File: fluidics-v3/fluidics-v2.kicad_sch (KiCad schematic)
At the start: 33 parts, among them J1 PJ-063AH, J10 87832-1010, J11 0705430001, J12 87832-1010, J13 0705430001, J14 87832-1010, J15 0533980671, J16 0705430001, J17 0533980671, J18 87832-1010, J19 0705430001, J2 B6B-ZR-SM4-TF, J20 0533980671, J21 87832-1010, J22 0705430001, J24 0705430001, J25 87832-1010, J3 A-DS_15_A_KG-T4S, J4 B6B-ZR-SM4-TF, U2 Teensy4.1

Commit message: Add GPIO_5 status LED and +24V screw terminal J7
- Root sheet: GPIO_5 status LED (D12 + R12 2.7K to GND)
- Solenoid driver sheet: J7 2-pin screw terminal (pin2 = +24V)

Schematic parses clean via kicad-cli; D12/R12/J7 present in netlist.

Co-Authored-By: Claude Opus 4.8 (1M context) <noreply@anthropic.com>
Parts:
- added D12: LED, LED_SMD:LED_0402_1005Metric, symbol Device:LED
- added R12: 2.7K, Resistor_SMD:R_0402_1005Metric, symbol Device:R
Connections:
- net GND: now also D12.1 (K)
- net GPIO_5: now also R12.1
- new net: D12.2 (A), R12.2

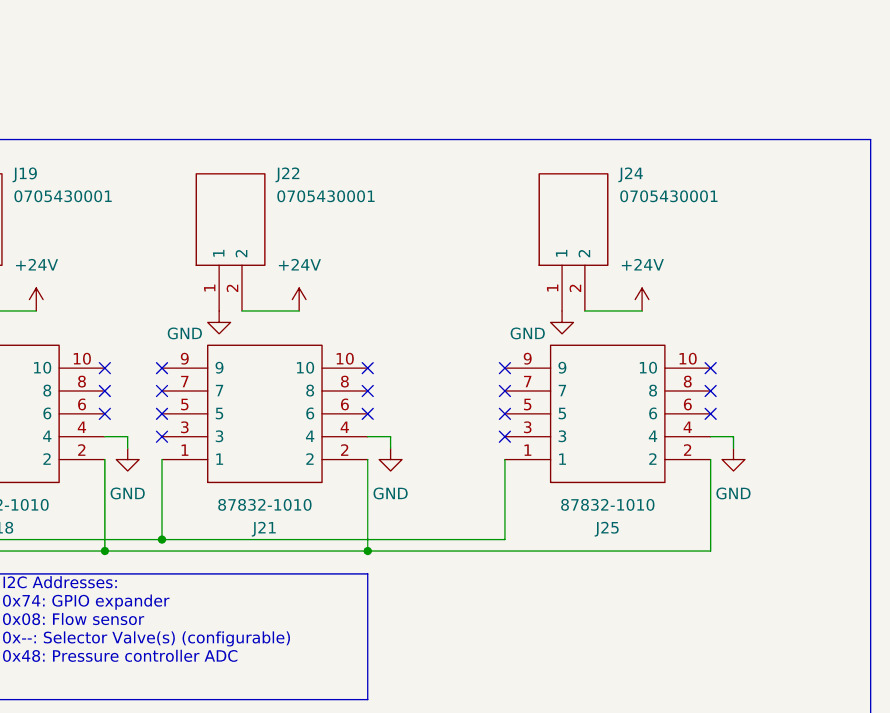
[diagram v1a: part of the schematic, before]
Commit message: Consolidate solenoid outputs to single 1x06 terminal J5
Replace 3x 1x02 blocks (J5/J6/J7) with one 6-position Xinya XY308-2.54-6P
(J5): pads 1/3/5 = U1 TPL7407 OUT5/6/7, pads 2/4/6 = +24V. DRC electrically
clean (0 clearance/shorting; 5 unconnected are intentional U2 GPIO/SPI NC).

Assign 3D model: KiCad 10 ships no Xinya XY308 .step, so point J5's model at
the bundled Phoenix MPT-0,5-6-2.54 1x06 (same pitch/positions) for the 3D
preview. Footprint/BOM/CPL still reference the real Xinya part.

Co-Authored-By: Claude Opus 4.8 (1M context) <noreply@anthropic.com>
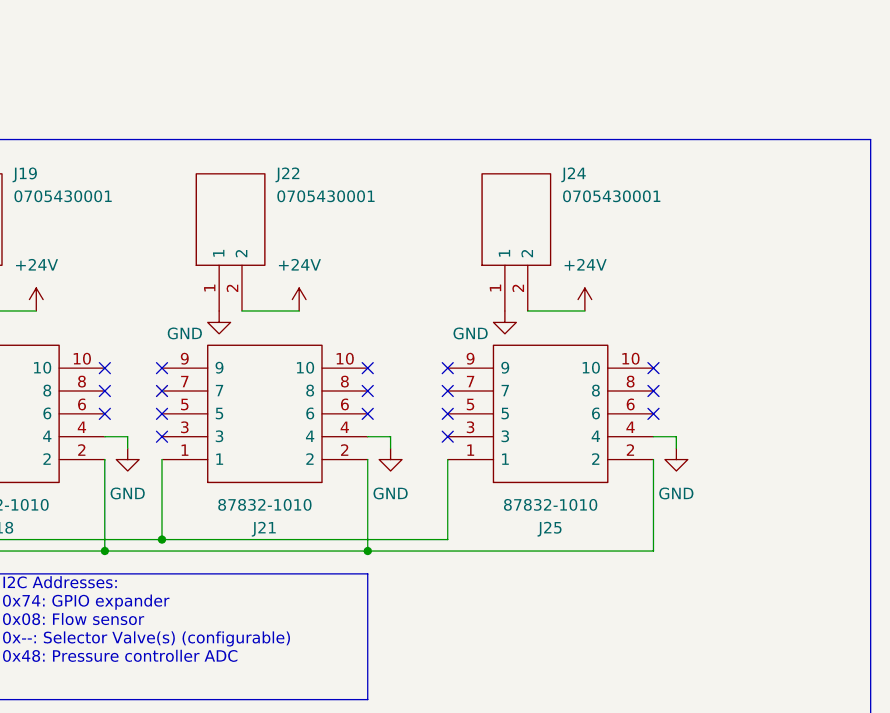
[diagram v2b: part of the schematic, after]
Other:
- moved on the sheet: J24, J25
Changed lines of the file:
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@@
 	)
 	(no_connect
-		(at 388.62 85.09)
+		(at 382.27 85.09)
 	)
 	(no_connect
@@
 	)
 	(no_connect
-		(at 365.76 90.17)
+		(at 359.41 90.17)
 	)
 	(no_connect
@@
 	)
 	(no_connect
-		(at 365.76 87.63)
+		(at 359.41 87.63)
 	)
 	(no_connect
@@
 	)
 	(no_connect
-		(at 388.62 87.63)
+		(at 382.27 87.63)
 	)
 	(no_connect
@@
 	)
 	(no_connect
-		(at 365.76 92.71)
+		(at 359.41 92.71)
 	)
 	(no_connect
@@
 	)
 	(no_connect
-		(at 388.62 90.17)
+		(at 382.27 90.17)
 	)
 	(no_connect
-		(at 365.76 85.09)
+		(at 359.41 85.09)
 	)
 	(no_connect
@@
 	(wire
 		(pts
-			(xy 391.16 92.71) (xy 388.62 92.71)
+			(xy 384.81 92.71) (xy 382.27 92.71)
 		)
 		(stroke
@@
 	(wire
 		(pts
-			(xy 350.52 105.41) (xy 388.62 105.41)
+			(xy 350.52 105.41) (xy 382.27 105.41)
 		)
 		(stroke
@@
 	(wire
 		(pts
-			(xy 374.65 78.74) (xy 381 78.74)
+			(xy 368.3 78.74) (xy 374.65 78.74)
 		)
 		(stroke
@@
 	(wire
 		(pts
-			(xy 365.76 104.14) (xy 365.76 95.25)
+			(xy 359.41 104.14) (xy 359.41 95.25)
 		)
 		(stroke
@@
 	(wire
 		(pts
-			(xy 391.16 92.71) (xy 391.16 93.98)
+			(xy 384.81 92.71) (xy 384.81 93.98)
 		)
 		(stroke
@@
 	(wire
 		(pts
-			(xy 327.66 104.14) (xy 365.76 104.14)
+			(xy 327.66 104.14) (xy 359.41 104.14)
 		)
 		(stroke
@@
 	(wire
 		(pts
-			(xy 388.62 105.41) (xy 388.62 95.25)
+			(xy 382.27 105.41) (xy 382.27 95.25)
 		)
 		(stroke
@@
 	(symbol
 		(lib_id "0705430001:0705430001")
-		(at 372.11 78.74 90)
+		(at 365.76 78.74 90)
 		(unit 1)
 		(body_style 1)
@@
 		(dnp no)
 		(property "Reference" "J24"
-			(at 378.46 63.5 90)
+			(at 372.11 63.5 90)
 			(show_name no)
 			(do_not_autoplace no)
@@
 		)
 		(property "Value" "0705430001"
-			(at 378.46 66.04 90)
+			(at 372.11 66.04 90)
 			(show_name no)
 			(do_not_autoplace no)
@@
 		)
 		(property "Footprint" "molex_connectors:SHDR2W64P0X254_1X2_737X660X1181P"
-			(at 369.57 62.23 0)
+			(at 363.22 62.23 0)
 			(hide yes)
 			(show_name no)
@@
 		)
 		(property "Datasheet" "https://www.molex.com/webdocs/datasheets/pdf/en-us/0705430001_PCB_HEADERS.pdf"
-			(at 372.11 62.23 0)
+			(at 365.76 62.23 0)
 			(hide yes)
 			(show_name no)
@@
 		)
 		(property "Description" "Headers & Wire Housings SL 2.54MM HDR VT TH SHRD 1X02P"
-			(at 374.65 62.23 0)
+			(at 368.3 62.23 0)
 			(hide yes)
 			(show_name no)
@@
 		)
 		(property "Height" "11.81"
-			(at 377.19 62.23 0)
+			(at 370.84 62.23 0)
 			(hide yes)
 			(show_name no)
@@
 		)
 		(property "Manufacturer_Name" "Molex"
-			(at 379.73 62.23 0)
+			(at 373.38 62.23 0)
 			(hide yes)
 			(show_name no)
@@
 		)
 		(property "Manufacturer_Part_Number" "0705430001"
-			(at 382.27 62.23 0)
+			(at 375.92 62.23 0)
 			(hide yes)
 			(show_name no)
@@
 		)
 		(property "Mouser Part Number" "N/A"
-			(at 384.81 62.23 0)
+			(at 378.46 62.23 0)
 			(hide yes)
 			(show_name no)
@@
 		)
 		(property "Mouser Price/Stock" "https://www.mouser.co.uk/ProductDetail/Molex/0705430001?qs=PBcRNPEHKsrZYrVlaLTOSA%3D%3D"
-			(at 387.35 62.23 0)
+			(at 381 62.23 0)
 			(hide yes)
 			(show_name no)
@@
 		)
 		(property "Arrow Part Number" "0705430001"
-			(at 389.89 62.23 0)
+			(at 383.54 62.23 0)
 			(hide yes)
 			(show_name no)
@@
 		)
 		(property "Arrow Price/Stock" "https://www.arrow.com/en/products/0705430001/molex"
-			(at 392.43 62.23 0)
+			(at 386.08 62.23 0)
 			(hide yes)
 			(show_name no)
@@
 	(symbol
 		(lib_id "87832-1010:87832-1010")
-		(at 365.76 95.25 0)
+		(at 359.41 95.25 0)
 		(mirror x)
 		(unit 1)
@@
 		(fields_autoplaced yes)
 		(property "Reference" "J25"
-			(at 377.19 102.87 0)
+			(at 370.84 102.87 0)
 			(show_name no)
 			(do_not_autoplace no)
@@
 		)
 		(property "Value" "87832-1010"
-			(at 377.19 100.33 0)
+			(at 370.84 100.33 0)
 			(show_name no)
 			(do_not_autoplace no)
@@
 		)
 		(property "Footprint" "molex_connectors:878321010"
-			(at 384.81 97.79 0)
+			(at 378.46 97.79 0)
 			(hide yes)
 			(show_name no)
@@
 		)
 		(property "Datasheet" "https://www.mouser.com/datasheet/2/276/0878321010_PCB_HEADERS-176533.pdf"
-			(at 384.81 95.25 0)
+			(at 378.46 95.25 0)
 			(hide yes)
 			(show_name no)
@@
 		)
 		(property "Description" "Molex Milli-Grid 87832, 10 Way, 2 Row, Straight PCB Header"
-			(at 384.81 92.71 0)
+			(at 378.46 92.71 0)
 			(hide yes)
 			(show_name no)
@@
 		)
 		(property "Height" "6.6"
-			(at 384.81 90.17 0)
+			(at 378.46 90.17 0)
 			(hide yes)
 			(show_name no)
@@
 		)
 		(property "Manufacturer_Name" "Molex"
-			(at 384.81 87.63 0)
+			(at 378.46 87.63 0)
 			(hide yes)
 			(show_name no)
@@
 		)
 		(property "Manufacturer_Part_Number" "87832-1010"
-			(at 384.81 85.09 0)
+			(at 378.46 85.09 0)
 			(hide yes)
 			(show_name no)
@@
 		)
 		(property "Mouser Part Number" "538-87832-1010"
-			(at 384.81 82.55 0)
+			(at 378.46 82.55 0)
 			(hide yes)
 			(show_name no)
@@
 		)
 		(property "Mouser Price/Stock" "https://www.mouser.co.uk/ProductDetail/Molex/87832-1010/?qs=vZWlbdSpF0HlUzduEf8ttg%3D%3D"
-			(at 384.81 80.01 0)
+			(at 378.46 80.01 0)
 			(hide yes)
 			(show_name no)
@@
 		)
 		(property "Arrow Part Number" ""
-			(at 384.81 77.47 0)
+			(at 378.46 77.47 0)
 			(hide yes)
 			(show_name no)
@@
 		)
 		(property "Arrow Price/Stock" ""
-			(at 384.81 74.93 0)
+			(at 378.46 74.93 0)
 			(hide yes)
 			(show_name no)
@@
 	(symbol
 		(lib_id "power:GND")
-		(at 372.11 78.74 0)
+		(at 365.76 78.74 0)
 		(unit 1)
 		(body_style 1)
@@
 		(dnp no)
 		(property "Reference" "#PWR080"
-			(at 372.11 85.09 0)
+			(at 365.76 85.09 0)
 			(hide yes)
 			(show_name no)
@@
 		)
 		(property "Value" "GND"
-			(at 368.3 81.28 0)
+			(at 361.95 81.28 0)
 			(show_name no)
 			(do_not_autoplace no)
@@
 		)
 		(property "Footprint" ""
-			(at 372.11 78.74 0)
+			(at 365.76 78.74 0)
 			(hide yes)
 			(show_name no)
@@
 		)
 		(property "Datasheet" ""
-			(at 372.11 78.74 0)
+			(at 365.76 78.74 0)
 			(hide yes)
 			(show_name no)
@@
 		)
 		(property "Description" ""
-			(at 372.11 78.74 0)
+			(at 365.76 78.74 0)
 			(show_name no)
 			(do_not_autoplace no)
@@
 	(symbol
 		(lib_id "power:+24V")
-		(at 381 78.74 0)
+		(at 374.65 78.74 0)
 		(unit 1)
 		(body_style 1)
@@
 		(fields_autoplaced yes)
 		(property "Reference" "#PWR081"
-			(at 381 82.55 0)
+			(at 374.65 82.55 0)
 			(hide yes)
 			(show_name no)
@@
 		)
 		(property "Value" "+24V"
-			(at 381 73.66 0)
+			(at 374.65 73.66 0)
 			(show_name no)
 			(do_not_autoplace no)
@@
 		)
 		(property "Footprint" ""
-			(at 381 78.74 0)
+			(at 374.65 78.74 0)
 			(hide yes)
 			(show_name no)
@@
 		)
 		(property "Datasheet" ""
-			(at 381 78.74 0)
+			(at 374.65 78.74 0)
 			(hide yes)
 			(show_name no)
@@
 		)
 		(property "Description" ""
-			(at 381 78.74 0)
+			(at 374.65 78.74 0)
 			(show_name no)
 			(do_not_autoplace no)
@@
 	(symbol
 		(lib_id "power:GND")
-		(at 391.16 93.98 0)
+		(at 384.81 93.98 0)
 		(mirror y)
 		(unit 1)
@@
 		(fields_autoplaced yes)
 		(property "Reference" "#PWR082"
-			(at 391.16 100.33 0)
+			(at 384.81 100.33 0)
 			(hide yes)
 			(show_name no)
@@
 		)
 		(property "Value" "GND"
-			(at 391.16 99.06 0)
+			(at 384.81 99.06 0)
 			(show_name no)
 			(do_not_autoplace no)
@@
 		)
 		(property "Footprint" ""
-			(at 391.16 93.98 0)
+			(at 384.81 93.98 0)
 			(hide yes)
 			(show_name no)
@@
 		)
 		(property "Datasheet" ""
-			(at 391.16 93.98 0)
+			(at 384.81 93.98 0)
 			(hide yes)
 			(show_name no)
@@
 		)
 		(property "Description" ""
-			(at 391.16 93.98 0)
+			(at 384.81 93.98 0)
 			(show_name no)
 			(do_not_autoplace no)

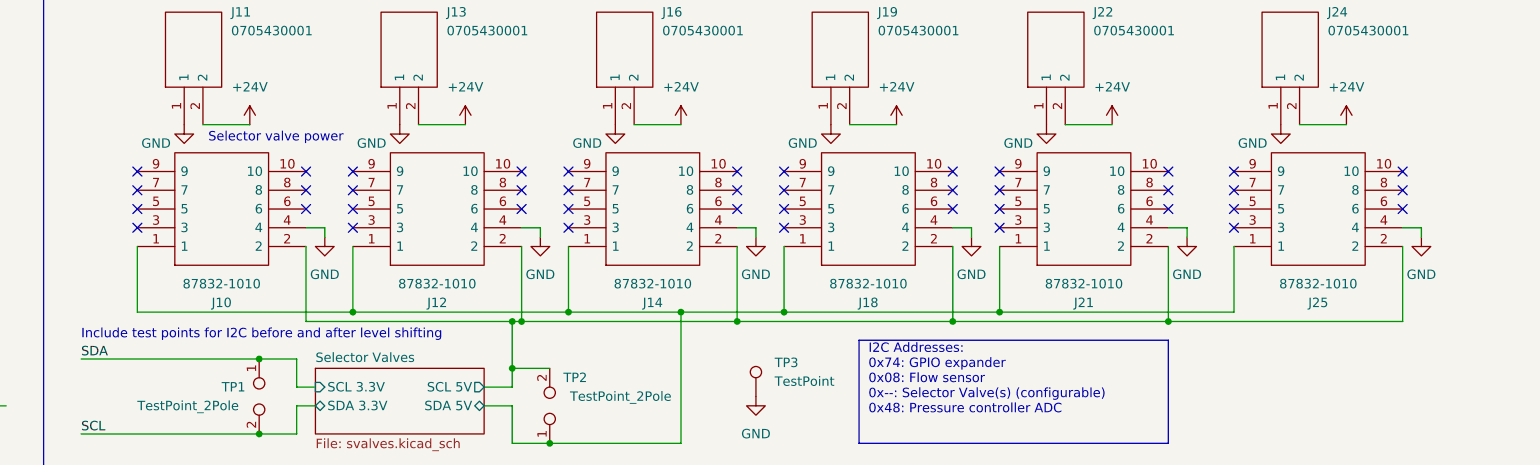
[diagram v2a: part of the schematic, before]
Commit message: v3 PCB: 3.3V power-plane islands + B.Cu bridge, refdes to F.Fab, block silk labels
PCB (this session, verified DRC-clean, 0 electrical regressions):
- Add +3.3V copper islands on In2.Cu (top U11/IC2 cluster + LDO/I2C-connector corner)
- Add +3.3V bridge pour on B.Cu down the inter-island corridor; delete ~18mm redundant vertical run
- Stitch 3.3V loads to islands with vias; remove ~35mm circuitous surface routing (3.3V trace 194->68mm)
- Move 21 hidden reference designators (caps, R22/R23/R51, U2 Teensy) to F.Fab, centered
- Add functional F.Silkscreen labels: Solenoid Driver, Flow, I2C Iso, RS-232

Also bundles accompanying schematic/library work not authored this session
(fluidics-v2.kicad_sch, svalves, solenoid_driver, 87832-0410 Molex connector lib).

Co-Authored-By: Claude Opus 4.8 (1M context) <noreply@anthropic.com>
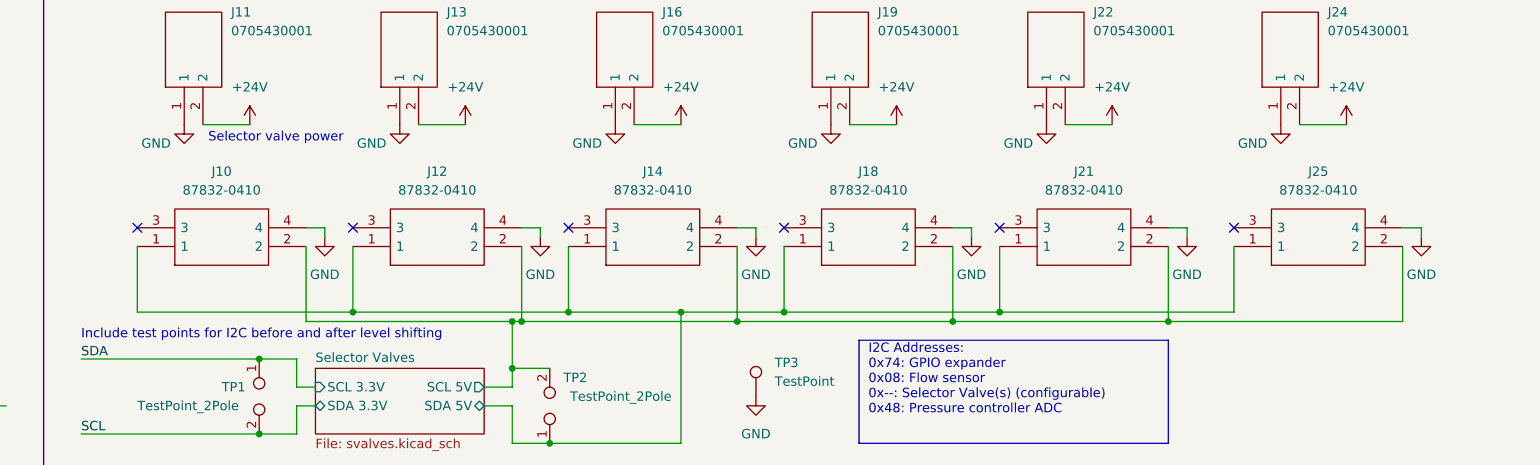
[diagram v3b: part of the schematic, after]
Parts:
- J10, J12, J14, J18, J21, J25: value 87832-1010 -> 87832-0410; footprint molex_connectors:878321010 -> molex_connectors:878320410; symbol 87832-1010:87832-1010 -> 87832-0410:87832-0410; Description_1 (none) -> Molex Milli-Grid 87832, 4 Way, 2 Row, Straight PCB Header; Manufacturer_Part_Number 87832-1010 -> 87832-0410
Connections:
- no-connect marks 83 -> 47
